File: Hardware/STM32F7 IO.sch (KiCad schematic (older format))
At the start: 19 parts, among them U16 STM32F765ZGT6

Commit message: Reconfiguring pinout round 2
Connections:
- net SPI4_MISO is gone; now on net OC11: U16.66 (PE13)
- net SPI4_MOSI is gone; now on net OC12: U16.67 (PE14)
- net OC10: now also U16.64 (PE11); no longer U16.101 (PA9)
- net OC11: no longer U16.102 (PA10)
- net OC12: no longer U16.103 (PA11)
- net PPM: now also U16.41 (PA5); no longer U16.34 (PA0)
- net SPI1_MISO: now also U16.124 (PG9); no longer U16.42 (PA6)
- net SPI1_MOSI: now also U16.123 (PD7); no longer U16.43 (PA7)
- net SPI1_SCK: now also U16.126 (PG11); no longer U16.41 (PA5)
- net UART4_RX: now also U16.35 (PA1); no longer U16.114 (PD0)
- net UART4_TX: now also U16.34 (PA0); no longer U16.115 (PD1)
- net UART1_RTS: now reaches U16.104 (PA12)
- net JRST: now reaches U16.134 (PB4)
- net SPI2_SCK: now reaches U16.69 (PB10)
- net SPI2_NSS: now reaches U16.73 (PB12)
- net SPI2_MISO: now reaches U16.28 (PC2)
- net SPI2_MOSI: now reaches U16.29 (PC3)
- net UART7_RTS: now reaches U16.60 (PE9)
- net UART7_CTS: now reaches U16.63 (PE10)
- net SPI5_NSS: now reaches U16.18 (PF6)
- net SPI1_NSS: now reaches U16.125 (PG10)
- net SPI3_MISO: no longer names the net of U16.112 (PC11)
- net SPI3_MOSI: no longer names the net of U16.113 (PC12)
- net SPI3_SCK: no longer names the net of U16.111 (PC10)
- net SPI4_SCK: no longer names the net of U16.65 (PE12)
- net TRACECLK: no longer names the net of U16.1 (PE2)
- net TRACED0: no longer names the net of U16.2 (PE3)
- net TRACED1: no longer names the net of U16.3 (PE4)
- net TRACED2: no longer names the net of U16.4 (PE5)
- net TRACED3: no longer names the net of U16.5 (PE6)
- net USART1_RX renamed UART4_RTS
- net USART1_TX renamed UART4_CTS
- new net UART1_CTS: U16.103 (PA11)
- new net UART1_RX: U16.102 (PA10)
- new net UART1_TX: U16.101 (PA9)
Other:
- note removed: "JTAG"

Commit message: first rough draft without headers
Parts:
- gave numbers to parts that had none: 18

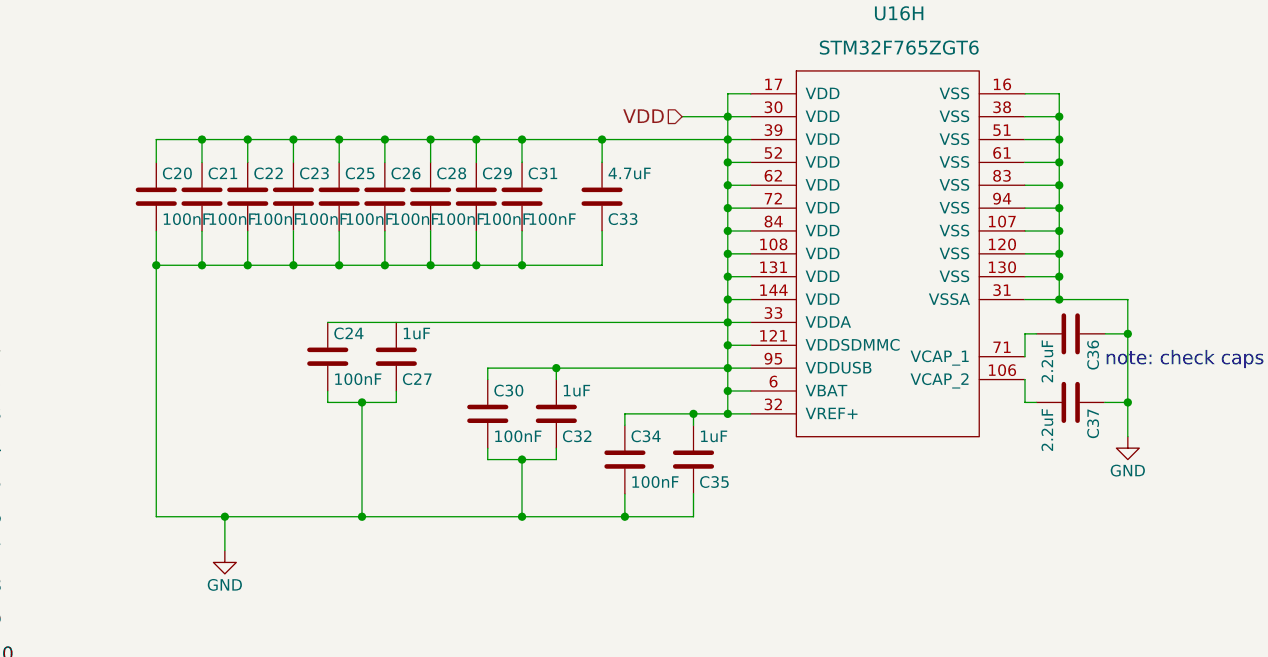
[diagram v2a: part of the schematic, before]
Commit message: branch to make PR for review
I should have made a separate branch for the development and then merged
it, but its too late now.
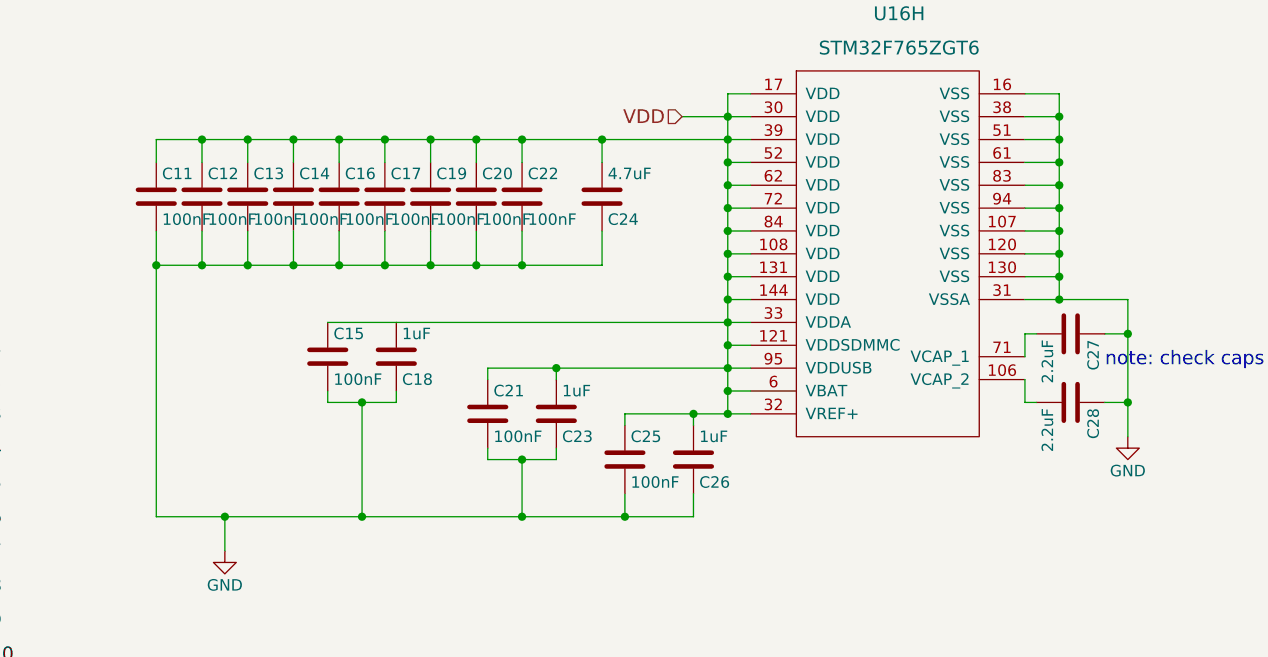
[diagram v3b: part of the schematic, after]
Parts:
- renumbered C20 to C11, C21 to C12, C22 to C13, C23 to C14, C24 to C15, C25 to C16, C26 to C17, C27 to C18, C28 to C19, C29 to C20, C30 to C21, C31 to C22, C32 to C23, C33 to C24, C34 to C25, C35 to C26, C36 to C27, C37 to C28
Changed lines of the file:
@@
 todo- boot pin?
 $Comp
-L C C36
+L C C27
 U 1 1 591E50BB
 P 10350 5550
-F 0 "C36" H 10375 5650 50  0000 L CNN
+F 0 "C27" H 10375 5650 50  0000 L CNN
 F 1 "2.2uF" H 10375 5450 50  0000 L CNN
 F 2 "" H 10388 5400 50  0001 C CNN
@@
 $EndComp
 $Comp
-L C C37
+L C C28
 U 1 1 591E50F4
 P 10350 5850
-F 0 "C37" H 10375 5950 50  0000 L CNN
+F 0 "C28" H 10375 5950 50  0000 L CNN
 F 1 "2.2uF" H 10375 5750 50  0000 L CNN
 F 2 "" H 10388 5700 50  0001 C CNN
@@
 $EndComp
 $Comp
-L GND #PWR039
+L GND #PWR40
 U 1 1 591E59BE
 P 10600 6000
-F 0 "#PWR039" H 10600 5750 50  0001 C CNN
+F 0 "#PWR40" H 10600 5750 50  0001 C CNN
 F 1 "GND" H 10600 5850 50  0000 C CNN
 F 2 "" H 10600 6000 50  0001 C CNN
@@
 $EndComp
 $Comp
-L C C20
+L C C11
 U 1 1 591E6705
 P 6350 4950
-F 0 "C20" H 6375 5050 50  0000 L CNN
+F 0 "C11" H 6375 5050 50  0000 L CNN
 F 1 "100nF" H 6375 4850 50  0000 L CNN
 F 2 "" H 6388 4800 50  0001 C CNN
@@
 $EndComp
 $Comp
-L C C21
+L C C12
 U 1 1 591E674D
 P 6550 4950
-F 0 "C21" H 6575 5050 50  0000 L CNN
+F 0 "C12" H 6575 5050 50  0000 L CNN
 F 1 "100nF" H 6575 4850 50  0000 L CNN
 F 2 "" H 6588 4800 50  0001 C CNN
@@
 $EndComp
 $Comp
-L C C22
+L C C13
 U 1 1 591E6786
 P 6750 4950
-F 0 "C22" H 6775 5050 50  0000 L CNN
+F 0 "C13" H 6775 5050 50  0000 L CNN
 F 1 "100nF" H 6775 4850 50  0000 L CNN
 F 2 "" H 6788 4800 50  0001 C CNN
@@
 $EndComp
 $Comp
-L C C23
+L C C14
 U 1 1 591E67C0
 P 6950 4950
-F 0 "C23" H 6975 5050 50  0000 L CNN
+F 0 "C14" H 6975 5050 50  0000 L CNN
 F 1 "100nF" H 6975 4850 50  0000 L CNN
 F 2 "" H 6988 4800 50  0001 C CNN
@@
 $EndComp
 $Comp
-L C C25
+L C C16
 U 1 1 591E67F2
 P 7150 4950
-F 0 "C25" H 7175 5050 50  0000 L CNN
+F 0 "C16" H 7175 5050 50  0000 L CNN
 F 1 "100nF" H 7175 4850 50  0000 L CNN
 F 2 "" H 7188 4800 50  0001 C CNN
@@
 $EndComp
 $Comp
-L C C26
+L C C17
 U 1 1 591E682B
 P 7350 4950
-F 0 "C26" H 7375 5050 50  0000 L CNN
+F 0 "C17" H 7375 5050 50  0000 L CNN
 F 1 "100nF" H 7375 4850 50  0000 L CNN
 F 2 "" H 7388 4800 50  0001 C CNN
@@
 $EndComp
 $Comp
-L C C28
+L C C19
 U 1 1 591E6860
 P 7550 4950
-F 0 "C28" H 7575 5050 50  0000 L CNN
+F 0 "C19" H 7575 5050 50  0000 L CNN
 F 1 "100nF" H 7575 4850 50  0000 L CNN
 F 2 "" H 7588 4800 50  0001 C CNN
@@
 $EndComp
 $Comp
-L C C29
+L C C20
 U 1 1 591E689D
 P 7750 4950
-F 0 "C29" H 7775 5050 50  0000 L CNN
+F 0 "C20" H 7775 5050 50  0000 L CNN
 F 1 "100nF" H 7775 4850 50  0000 L CNN
 F 2 "" H 7788 4800 50  0001 C CNN
@@
 $EndComp
 $Comp
-L C C31
+L C C22
 U 1 1 591E68E4
 P 7950 4950
-F 0 "C31" H 7975 5050 50  0000 L CNN
+F 0 "C22" H 7975 5050 50  0000 L CNN
 F 1 "100nF" H 7975 4850 50  0000 L CNN
 F 2 "" H 7988 4800 50  0001 C CNN
@@
 $EndComp
 $Comp
-L C C33
+L C C24
 U 1 1 591E794E
 P 8300 4950
-F 0 "C33" H 8325 5050 50  0000 L CNN
+F 0 "C24" H 8325 5050 50  0000 L CNN
 F 1 "4.7uF" H 8325 4850 50  0000 L CNN
 F 2 "" H 8338 4800 50  0001 C CNN
@@
 $EndComp
 $Comp
-L C C30
+L C C21
 U 1 1 591E887D
 P 7800 5900
-F 0 "C30" H 7825 6000 50  0000 L CNN
+F 0 "C21" H 7825 6000 50  0000 L CNN
 F 1 "100nF" H 7825 5800 50  0000 L CNN
 F 2 "" H 7838 5750 50  0001 C CNN
@@
 $EndComp
 $Comp
-L C C32
+L C C23
 U 1 1 591E88F6
 P 8100 5900
-F 0 "C32" H 8125 6000 50  0000 L CNN
+F 0 "C23" H 8125 6000 50  0000 L CNN
 F 1 "1uF" H 8125 5800 50  0000 L CNN
 F 2 "" H 8138 5750 50  0001 C CNN
@@
 $EndComp
 $Comp
-L C C24
+L C C15
 U 1 1 591E9E4D
 P 7100 5650
-F 0 "C24" H 7125 5750 50  0000 L CNN
+F 0 "C15" H 7125 5750 50  0000 L CNN
 F 1 "100nF" H 7125 5550 50  0000 L CNN
 F 2 "" H 7138 5500 50  0001 C CNN
@@
 $EndComp
 $Comp
-L C C27
+L C C18
 U 1 1 591EA2B7
 P 7400 5650
-F 0 "C27" H 7425 5750 50  0000 L CNN
+F 0 "C18" H 7425 5750 50  0000 L CNN
 F 1 "1uF" H 7425 5550 50  0000 L CNN
 F 2 "" H 7438 5500 50  0001 C CNN
@@
 $EndComp
 $Comp
-L C C34
+L C C25
 U 1 1 591EA38F
 P 8400 6100
-F 0 "C34" H 8425 6200 50  0000 L CNN
+F 0 "C25" H 8425 6200 50  0000 L CNN
 F 1 "100nF" H 8425 6000 50  0000 L CNN
 F 2 "" H 8438 5950 50  0001 C CNN
@@
 $EndComp
 $Comp
-L C C35
+L C C26
 U 1 1 591EA3F9
 P 8700 6100
-F 0 "C35" H 8725 6200 50  0000 L CNN
+F 0 "C26" H 8725 6200 50  0000 L CNN
 F 1 "1uF" H 8725 6000 50  0000 L CNN
 F 2 "" H 8738 5950 50  0001 C CNN
@@
 $EndComp
 $Comp
-L GND #PWR040
+L GND #PWR39
 U 1 1 591EB43A
 P 6650 6500
-F 0 "#PWR040" H 6650 6250 50  0001 C CNN
+F 0 "#PWR39" H 6650 6250 50  0001 C CNN
 F 1 "GND" H 6650 6350 50  0000 C CNN
 F 2 "" H 6650 6500 50  0001 C CNN

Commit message: Added a lot of debug
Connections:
- net PG14: now reaches U16.129 (PG14)
- net PG15: now reaches U16.132 (PG15)
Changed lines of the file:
@@
 Connection ~ 7250 6350
 Wire Wire Line
-	7250 5850 7250 6350
+	7250 6350 7250 5850
 Connection ~ 7950 6100
 Connection ~ 7950 6350
 Wire Wire Line
-	7950 6100 7950 6350
+	7950 6350 7950 6100
 Connection ~ 6350 5250
 Connection ~ 8400 6350
 Wire Wire Line
-	8950 5300 8850 5300
+	8850 5300 8950 5300
 Wire Wire Line
 	7100 5850 7100 5800
 Wire Wire Line
-	7100 5850 7250 5850
-Wire Wire Line
-	7250 5850 7400 5850
+	7100 5850 7400 5850
 Wire Wire Line
 	7400 5850 7400 5800
@@
 	8700 6350 8700 6250
 Wire Wire Line
-	6350 6350 6650 6350
-Wire Wire Line
-	6650 6350 7250 6350
-Wire Wire Line
-	7250 6350 7950 6350
-Wire Wire Line
-	7950 6350 8400 6350
-Wire Wire Line
-	8400 6350 8700 6350
+	6350 6350 8700 6350
 Wire Wire Line
 	8400 6350 8400 6250
@@
 	7800 6100 7800 6050
 Wire Wire Line
-	7800 6100 7950 6100
-Wire Wire Line
-	7950 6100 8100 6100
+	7800 6100 8100 6100
 Wire Wire Line
 	8100 6100 8100 6050
 Connection ~ 8300 4700
 Wire Wire Line
-	8300 4800 8300 4700
+	8300 4700 8300 4800
 Connection ~ 7950 5250
 Wire Wire Line
@@
 Connection ~ 6750 5250
 Wire Wire Line
-	6750 5100 6750 5250
+	6750 5250 6750 5100
 Connection ~ 6950 5250
 Wire Wire Line
-	6950 5100 6950 5250
+	6950 5250 6950 5100
 Connection ~ 7150 5250
 Wire Wire Line
-	7150 5100 7150 5250
+	7150 5250 7150 5100
 Connection ~ 7350 5250
 Wire Wire Line
-	7350 5100 7350 5250
+	7350 5250 7350 5100
 Connection ~ 7550 5250
 Wire Wire Line
-	7550 5100 7550 5250
+	7550 5250 7550 5100
 Connection ~ 7750 5250
 Wire Wire Line
-	7750 5100 7750 5250
+	7750 5250 7750 5100
 Wire Wire Line
 	7950 5250 7950 5100
 Wire Wire Line
-	6350 5250 6550 5250
-Wire Wire Line
-	6550 5250 6750 5250
-Wire Wire Line
-	6750 5250 6950 5250
-Wire Wire Line
-	6950 5250 7150 5250
-Wire Wire Line
-	7150 5250 7350 5250
-Wire Wire Line
-	7350 5250 7550 5250
-Wire Wire Line
-	7550 5250 7750 5250
-Wire Wire Line
-	7750 5250 7950 5250
-Wire Wire Line
-	7950 5250 8300 5250
-Wire Wire Line
-	6350 5100 6350 5250
-Wire Wire Line
-	6350 5250 6350 6350
+	6350 5250 8300 5250
+Wire Wire Line
+	6350 5100 6350 6350
 Connection ~ 7950 4700
 Wire Wire Line
-	7950 4800 7950 4700
+	7950 4700 7950 4800
 Connection ~ 7750 4700
 Wire Wire Line
-	7750 4800 7750 4700
+	7750 4700 7750 4800
 Connection ~ 7550 4700
 Wire Wire Line
-	7550 4800 7550 4700
+	7550 4700 7550 4800
 Connection ~ 7350 4700
 Wire Wire Line
-	7350 4800 7350 4700
+	7350 4700 7350 4800
 Connection ~ 7150 4700
 Wire Wire Line
-	7150 4800 7150 4700
+	7150 4700 7150 4800
 Connection ~ 6950 4700
 Wire Wire Line
-	6950 4800 6950 4700
+	6950 4700 6950 4800
 Connection ~ 6750 4700
 Wire Wire Line
-	6750 4800 6750 4700
+	6750 4700 6750 4800
 Connection ~ 6550 4700
 Wire Wire Line
@@
 	10600 5850 10500 5850
 Wire Wire Line
-	10600 5400 10600 5550
-Wire Wire Line
-	10600 5550 10600 5850
-Wire Wire Line
-	10600 5850 10600 6000
+	10600 5400 10600 6000
 Wire Wire Line
 	10150 5550 10200 5550
@@
 Connection ~ 8850 5700
 Wire Wire Line
-	7800 5700 8100 5700
-Wire Wire Line
-	8100 5700 8850 5700
-Wire Wire Line
-	8850 5700 8950 5700
+	7800 5700 8950 5700
 Connection ~ 8850 5800
 Wire Wire Line
-	8400 5900 8700 5900
-Wire Wire Line
-	8700 5900 8850 5900
-Wire Wire Line
-	8850 5900 8950 5900
+	8400 5900 8950 5900
 Connection ~ 8850 5600
 Wire Wire Line
@@
 Connection ~ 8850 4600
 Wire Wire Line
-	8650 4600 8850 4600
-Wire Wire Line
-	8850 4600 8950 4600
+	8650 4600 8950 4600
 Connection ~ 8850 4700
 Connection ~ 8850 4800
 Wire Wire Line
-	8950 4800 8850 4800
+	8850 4800 8950 4800
 Connection ~ 8850 4900
 Wire Wire Line
-	8950 4900 8850 4900
+	8850 4900 8950 4900
 Connection ~ 8850 5000
 Wire Wire Line
-	8950 5000 8850 5000
+	8850 5000 8950 5000
 Connection ~ 8850 5100
 Wire Wire Line
-	8950 5100 8850 5100
+	8850 5100 8950 5100
 Connection ~ 8850 5200
 Wire Wire Line
-	8950 5200 8850 5200
+	8850 5200 8950 5200
 Connection ~ 8850 5300
 Wire Wire Line
-	6350 4700 6550 4700
-Wire Wire Line
-	6550 4700 6750 4700
-Wire Wire Line
-	6750 4700 6950 4700
-Wire Wire Line
-	6950 4700 7150 4700
-Wire Wire Line
-	7150 4700 7350 4700
-Wire Wire Line
-	7350 4700 7550 4700
-Wire Wire Line
-	7550 4700 7750 4700
-Wire Wire Line
-	7750 4700 7950 4700
-Wire Wire Line
-	7950 4700 8300 4700
-Wire Wire Line
-	8300 4700 8850 4700
-Wire Wire Line
-	8850 4700 8950 4700
+	6350 4700 8950 4700
 Connection ~ 8850 5400
 Wire Wire Line
-	8950 5400 8850 5400
-Wire Wire Line
-	7100 5500 8850 5500
-Wire Wire Line
-	8850 5500 8950 5500
-Wire Wire Line
-	8850 4500 8850 4600
-Wire Wire Line
-	8850 4600 8850 4700
-Wire Wire Line
-	8850 4700 8850 4800
-Wire Wire Line
-	8850 4800 8850 4900
-Wire Wire Line
-	8850 4900 8850 5000
-Wire Wire Line
-	8850 5000 8850 5100
-Wire Wire Line
-	8850 5100 8850 5200
-Wire Wire Line
-	8850 5200 8850 5300
-Wire Wire Line
-	8850 5300 8850 5400
-Wire Wire Line
-	8850 5400 8850 5500
-Wire Wire Line
-	8850 5500 8850 5600
-Wire Wire Line
-	8850 5600 8850 5700
-Wire Wire Line
-	8850 5700 8850 5800
-Wire Wire Line
-	8850 5800 8850 5900
+	8850 5400 8950 5400
+Wire Wire Line
+	7100 5500 8950 5500
+Wire Wire Line
+	8850 4500 8850 5900
 Wire Wire Line
 	8950 4500 8850 4500
@@
 Connection ~ 10300 4700
 Wire Wire Line
-	10150 4700 10300 4700
+	10300 4700 10150 4700
 Connection ~ 10300 4800
 Wire Wire Line
-	10150 4800 10300 4800
+	10300 4800 10150 4800
 Connection ~ 10300 4900
 Wire Wire Line
-	10150 4900 10300 4900
+	10300 4900 10150 4900
 Connection ~ 10300 5000
 Wire Wire Line
-	10150 5000 10300 5000
+	10300 5000 10150 5000
 Connection ~ 10300 5100
 Wire Wire Line
-	10150 5100 10300 5100
+	10300 5100 10150 5100
 Connection ~ 10300 5200
 Wire Wire Line
-	10150 5200 10300 5200
+	10300 5200 10150 5200
 Connection ~ 10300 5300
 Wire Wire Line
-	10150 5300 10300 5300
-Wire Wire Line
-	10150 5400 10300 5400
-Wire Wire Line
-	10300 5400 10600 5400
-Wire Wire Line
-	10300 4500 10300 4600
-Wire Wire Line
-	10300 4600 10300 4700
-Wire Wire Line
-	10300 4700 10300 4800
-Wire Wire Line
-	10300 4800 10300 4900
-Wire Wire Line
-	10300 4900 10300 5000
-Wire Wire Line
-	10300 5000 10300 5100
-Wire Wire Line
-	10300 5100 10300 5200
-Wire Wire Line
-	10300 5200 10300 5300
-Wire Wire Line
-	10300 5300 10300 5400
+	10300 5300 10150 5300
+Wire Wire Line
+	10150 5400 10600 5400
+Wire Wire Line
+	10300 4500 10300 5400
 Wire Wire Line
 	10150 4500 10300 4500
@@
 	5500 5650 5350 5650
 Wire Bus Line
-	5250 5550 5250 5700
-Wire Bus Line
-	5250 5700 5250 5850
-Wire Bus Line
-	5250 5850 5250 6000
-Wire Bus Line
-	5250 6000 5250 6150
-Wire Bus Line
-	5250 6150 5250 6300
-Wire Bus Line
-	5250 6300 5250 6450
-Wire Bus Line
-	5250 6450 5250 6600
-Wire Bus Line
-	5250 6600 5250 6750
-Wire Bus Line
-	5250 6750 5250 6900
-Wire Bus Line
-	5250 6900 5250 7050
-Wire Bus Line
-	5250 7050 5250 7200
+	5250 5550 5250 7200
 Wire Bus Line
 	5150 5450 5250 5550
 Wire Bus Line
 	5050 5450 5150 5450
+Text HLabel 10250 2050 2    60   Input ~ 0
+PG14
+Text HLabel 10250 2150 2    60   Input ~ 0
+PG15
+Wire Wire Line
+	10250 2050 10050 2050
+Wire Wire Line
+	10050 2150 10250 2150
 $EndSCHEMATC

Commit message: Fixed some BOM stuff
fixed BOM for non RLC components
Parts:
- added D17, D18, D19: LED, symbol LED
- added R54, R55, R56: 100, symbol R
- added SH?: SHORT, symbol SHORT
- U40: renamed from U16; part_num (none) -> CHIP-001
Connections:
- net labels added: PG13, SPI4_MISO, SPI4_MOSI, SPI4_NSS, SPI4_SCK, USART2_CTS, USART2_RTS
- net labels removed: ADC3_IN11
- wire segments 159 -> 183
- no-connect marks 0 -> 43
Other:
- note removed: "todo- boot pin?"
- moved on the sheet: C15, C18

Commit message: Finished RLC bom stuff
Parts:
- C11, C12, C13, C14, C15, C16, C17, C19, C20, C21, C22, C25: part_num (none) -> CAPP-005
- C18, C23, C26: part_num (none) -> CAPP-004
- C24: part_num (none) -> CAPP-006
- C27, C28: part_num (none) -> CAPP-007
- R54, R55, R56: part_num (none) -> RESS-006
- gave numbers to parts that had none: 1
- renumbered U40 to U16
